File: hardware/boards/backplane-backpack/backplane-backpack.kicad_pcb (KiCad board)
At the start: 2 copper layers, 151.8 x 30.8 mm, 0 parts

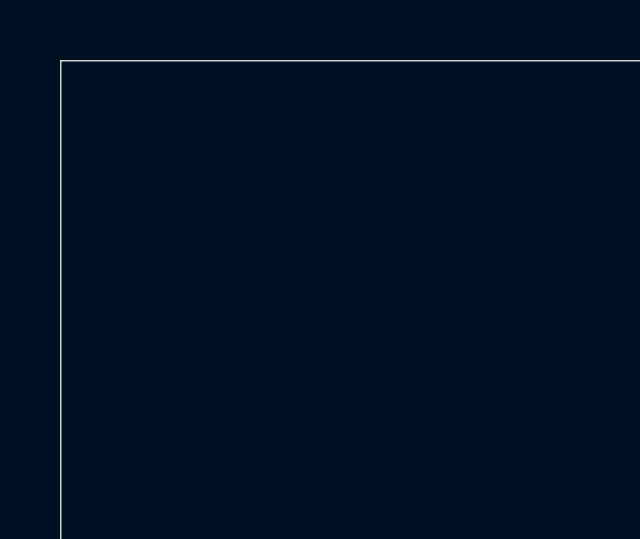
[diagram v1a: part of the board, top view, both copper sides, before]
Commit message: Simplify backpack backplane interface
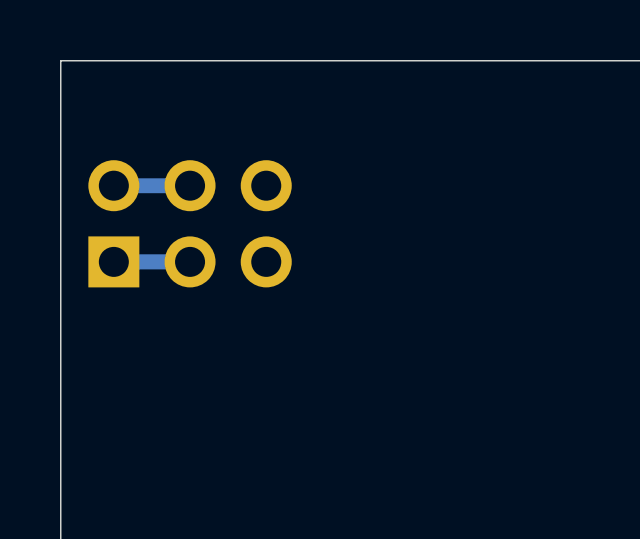
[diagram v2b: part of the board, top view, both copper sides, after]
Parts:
- added J11: backplane_mate, Connector_PinSocket_2.54mm:PinSocket_2x03_P2.54mm_Vertical, B.Cu at (31.3, 53.4)
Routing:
- net GND: track 0.00 -> 2.54 mm
- net +3V3: track 0.00 -> 2.54 mm
